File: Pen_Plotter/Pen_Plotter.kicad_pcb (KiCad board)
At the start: 2 copper layers, 74.8 x 35.8 mm, 35 parts, among them J1 USB4125-GF-A_REVA2, J2 PinHeader_01x05_P2.54mm_Verti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, J3 PinHeader_01x05_P2.54mm_Verti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, J4 Conn_02x03_Counter_Clockwise, J6 X Lim, J7 PinHeader_01x03_P2.54mm_Verti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, J8 X Lim, SW1 Reset-EN, SW2 Boot-GPIO0, U1 ESP32-WROOM-32E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

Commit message: PCB V2.1
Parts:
- removed R7: 0, fab:R_1206
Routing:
- net EN: track 58.7 -> 60.4 mm, vias 1 -> 2
- net ESP_RX: track 7.00 -> 7.62 mm, vias 0 -> 1
- net IN3: track 25.8 -> 25.2 mm
- net ESP_TX: track 7.53 -> 7.64 mm, vias 0 -> 1

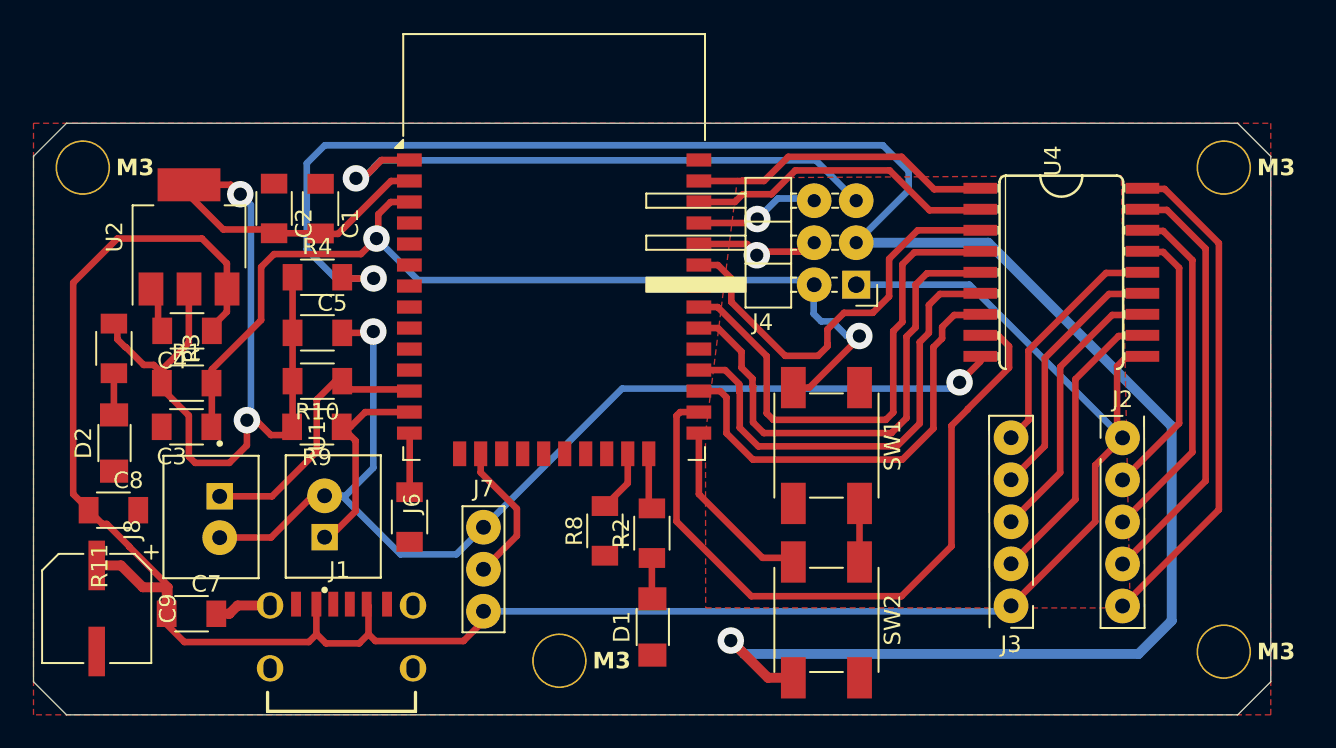
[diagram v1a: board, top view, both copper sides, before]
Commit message: Inverted IDC Connector position and thickened traces
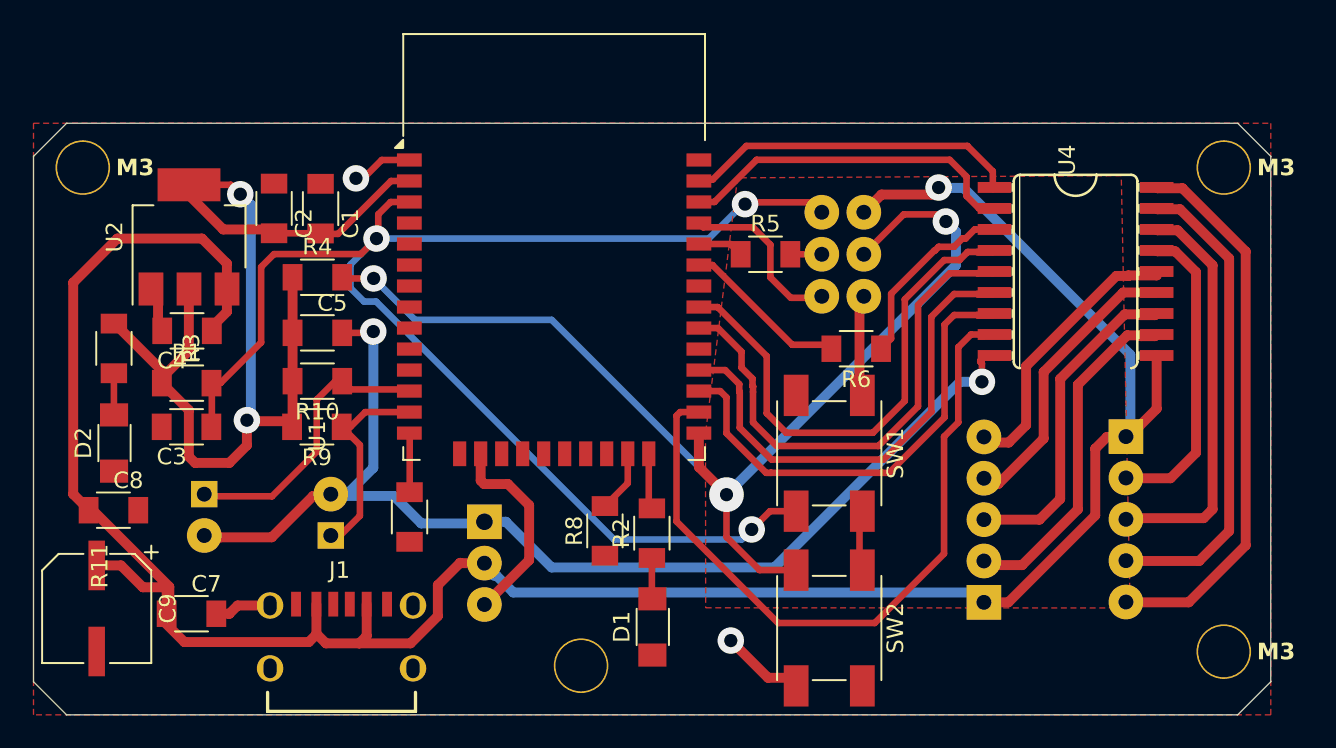
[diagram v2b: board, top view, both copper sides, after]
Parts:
- removed J7: PinHeader_01x03_P2.54mm_Vertical_THT_D1.4mm, fab:PinHeader_01x03_P2.54mm_Vertical_THT_D1.4mm
- added J5: 6120XX21621_61200621621, 6 Pin Male-Box Header:61200621621, B.Cu at (104.6, 100.0)
- added R5: R_1206, fab:R_1206, F.Cu at (99.9, 100.0)
- added R6: R_1206, fab:R_1206, F.Cu at (105.4, 105.7)
- H4, J6, J8: moved to B.Cu
- J2: value PinHeader_01x05_P2.54mm_Vertical_THT_D1.4mm -> Motor 1; footprint fab:PinHeader_01x05_P2.54mm_Vertical_THT_D1.4mm -> B5B-XH-A:JST_B5B-XH-A; moved to B.Cu
- J3: value PinHeader_01x05_P2.54mm_Vertical_THT_D1.4mm -> Motor 2; footprint fab:PinHeader_01x05_P2.54mm_Vertical_THT_D1.4mm -> B5B-XH-A:JST_B5B-XH-A; moved to B.Cu
- J4: value Conn_02x03_Counter_Clockwise -> Servo; footprint Connector_PinHeader_2.54mm:PinHeader_2x03_P2.54mm_Horizontal -> B3B-XH-A:JST_B3B-XH-A; moved to B.Cu
- moved J4 27.7 mm to (83.4, 118.6), turned to 90 degrees
- moved J3 5.64 mm to (112.6, 116.0), turned to -90 degrees
- moved J2 4.97 mm to (122.2, 116.0), turned to 90 degrees
- moved H4 1.34 mm to (88.7, 124.8), turned to 180 degrees
- moved U4 0.86 mm to (118.6, 101.0)
- moved J6 0.68 mm to (73.1, 115.7)
- moved SW2 0.52 mm to (103.7, 122.5)
- moved SW1 0.50 mm to (103.7, 112.0)
- moved J8 0.17 mm to (66.5, 115.7)
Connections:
- J4 pad 1: PWR_5V -> PWR_GND
- J4 pad 2: EN -> PWR_5V
- J4 pad 3: GPIO0 -> Servo
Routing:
- net GPIO0: track 134.1 -> 74.8 mm, vias 2 -> 4
- net EN: track 60.4 -> 88.3 mm, vias 2 -> 3
- net PWR_GND: track 112.7 -> 89.5 mm
- net PWR_5V: track 141.6 -> 152.3 mm, vias 0 -> 1
- net Servo: track 8.72 -> 12.4 mm
- net IN3: track 25.2 -> 21.5 mm
- net OUT3: track 21.3 -> 24.5 mm
- net OUT2: track 25.9 -> 29.1 mm
- net OUT1: track 30.3 -> 33.4 mm
- net OUT7: track 16.9 -> 19.9 mm
- net ESP_RX: track 7.62 -> 4.69 mm, vias 1 -> 0
- net ESP_TX: track 7.64 -> 10.5 mm, vias 1 -> 0
- net OUT8: track 17.9 -> 20.6 mm
- net OUT5: track 14.6 -> 17.1 mm
- net IN2: track 18.8 -> 21.0 mm
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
